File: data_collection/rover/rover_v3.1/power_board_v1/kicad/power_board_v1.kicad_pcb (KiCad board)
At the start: 2 copper layers, 90 x 65 mm, 131 parts, among them J1 XT60_BATT, J10 from Pi USB2, J11 UPDI prog (UPDI/3V3/GND), J12 XT30 fallback pads, J2 PANEL_SW, J3 USB4105-GF-A (TH shell), J4 USB_A radio1, J5 USB_A radio2, J6 AUX 5V 2A, J7 PI GPIO harness, J8 AUX_CTL out (JST-GH), J9 from Pi USB1, Q2 CSD18543Q3A diode, Q3 CSD18543Q3A switch, U1 LM5145 rail A, U2 LM5145 rail B, U3 ATtiny816 (VQFN), U4 LM74800-Q1, U5 INA226 (addr 0x40), U6 TPS7A1633 3V3 60V LDO, U7 TPS2553 1.7A, U8 TPS2553 1.7A, U9 AP2112K-3.3 (switched)

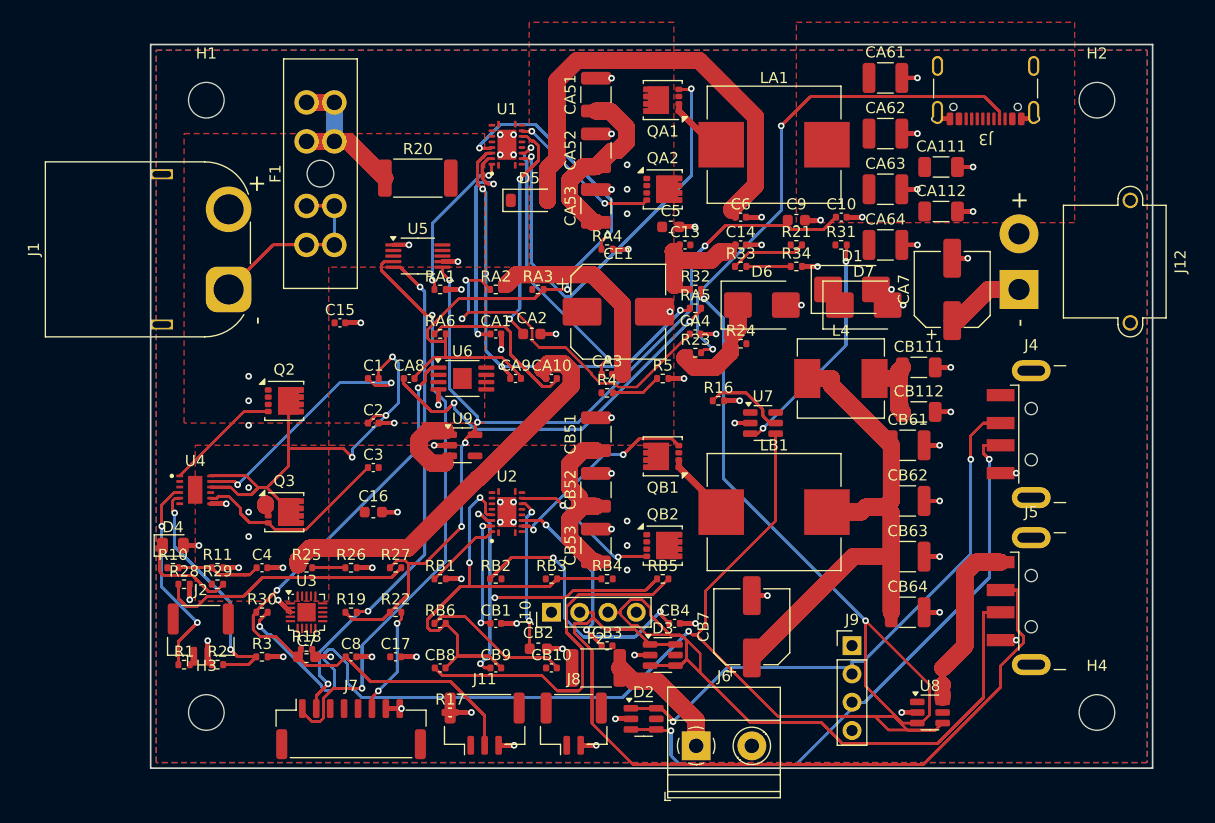
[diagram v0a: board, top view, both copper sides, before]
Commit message: Mounting pattern resolved: 3D-printed chassis adapter fits the board; corner M3 holes final
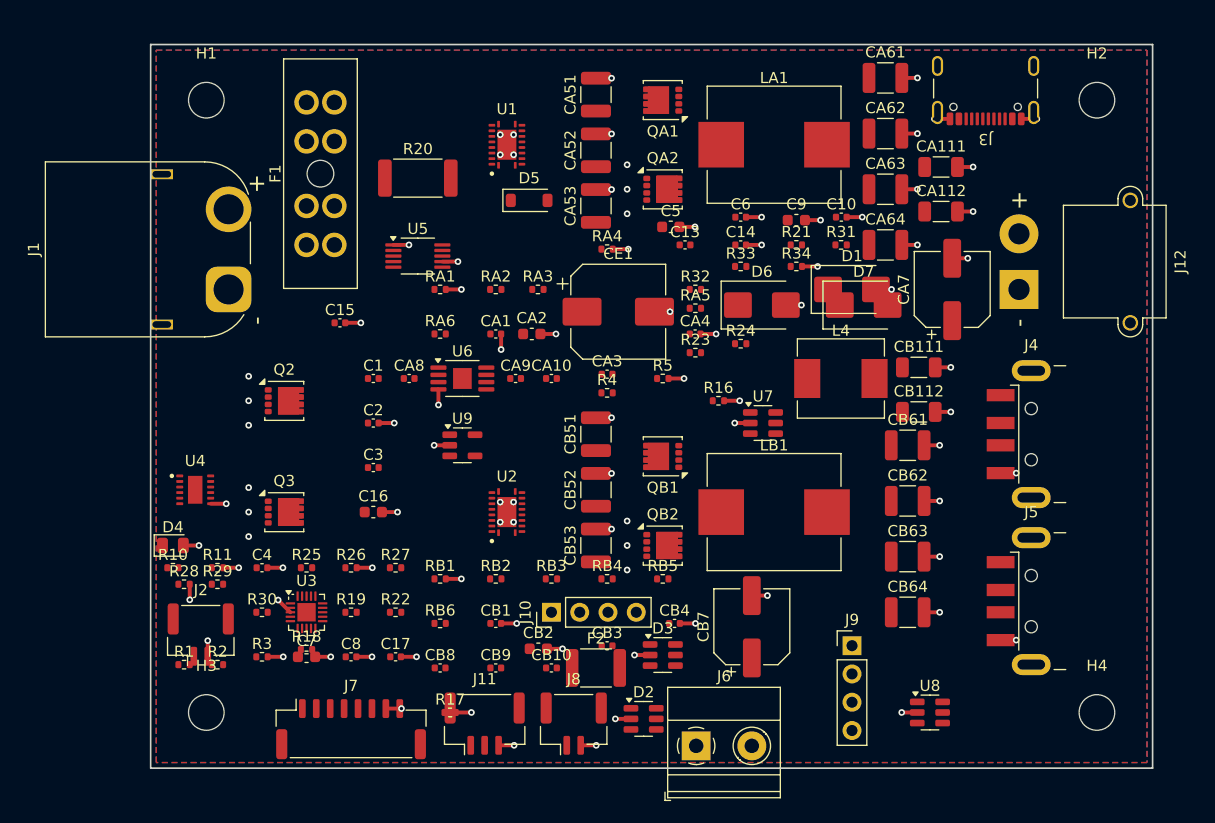
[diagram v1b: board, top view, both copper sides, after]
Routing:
- net GND: track 1576.1 -> 99.6 mm, vias 92 -> 91
- net FAULT_USB: track 762.8 -> 0.00 mm, vias 2 -> 0
- net 3V3_SW: track 631.5 -> 0.00 mm, vias 5 -> 0
- net D2_N: track 591.9 -> 0.00 mm
- net MCU_3V3: track 464.9 -> 0.00 mm, vias 2 -> 0
- net FB_A: track 463.4 -> 0.00 mm, vias 3 -> 0
- net D1_P: track 447.9 -> 0.00 mm, vias 2 -> 0
- net SDA: track 427.1 -> 0.00 mm, vias 2 -> 0
- net D2_P: track 420.1 -> 0.00 mm
- net D1_N: track 416.4 -> 0.00 mm, vias 2 -> 0
- net 5V_A: track 411.8 -> 0.00 mm
- net SCL: track 378.4 -> 0.00 mm, vias 3 -> 0
- net CC1_A: track 374.6 -> 0.00 mm, vias 2 -> 0
- net EN_USB2: track 359.1 -> 0.00 mm, vias 2 -> 0
- net 5VB_PRE: track 350.5 -> 0.00 mm
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- removed copper zone on F.Cu, net 5V_A
- removed copper zone on F.Cu, net VBATT_S
- removed copper zone on F.Cu, net VSW
